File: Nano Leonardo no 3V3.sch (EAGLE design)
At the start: 27 parts, among them U201 5V, U210 3.3V, U401 ATMEGA32U4, X1 USB_MICROB_JSTGCT, Y1 16MHz

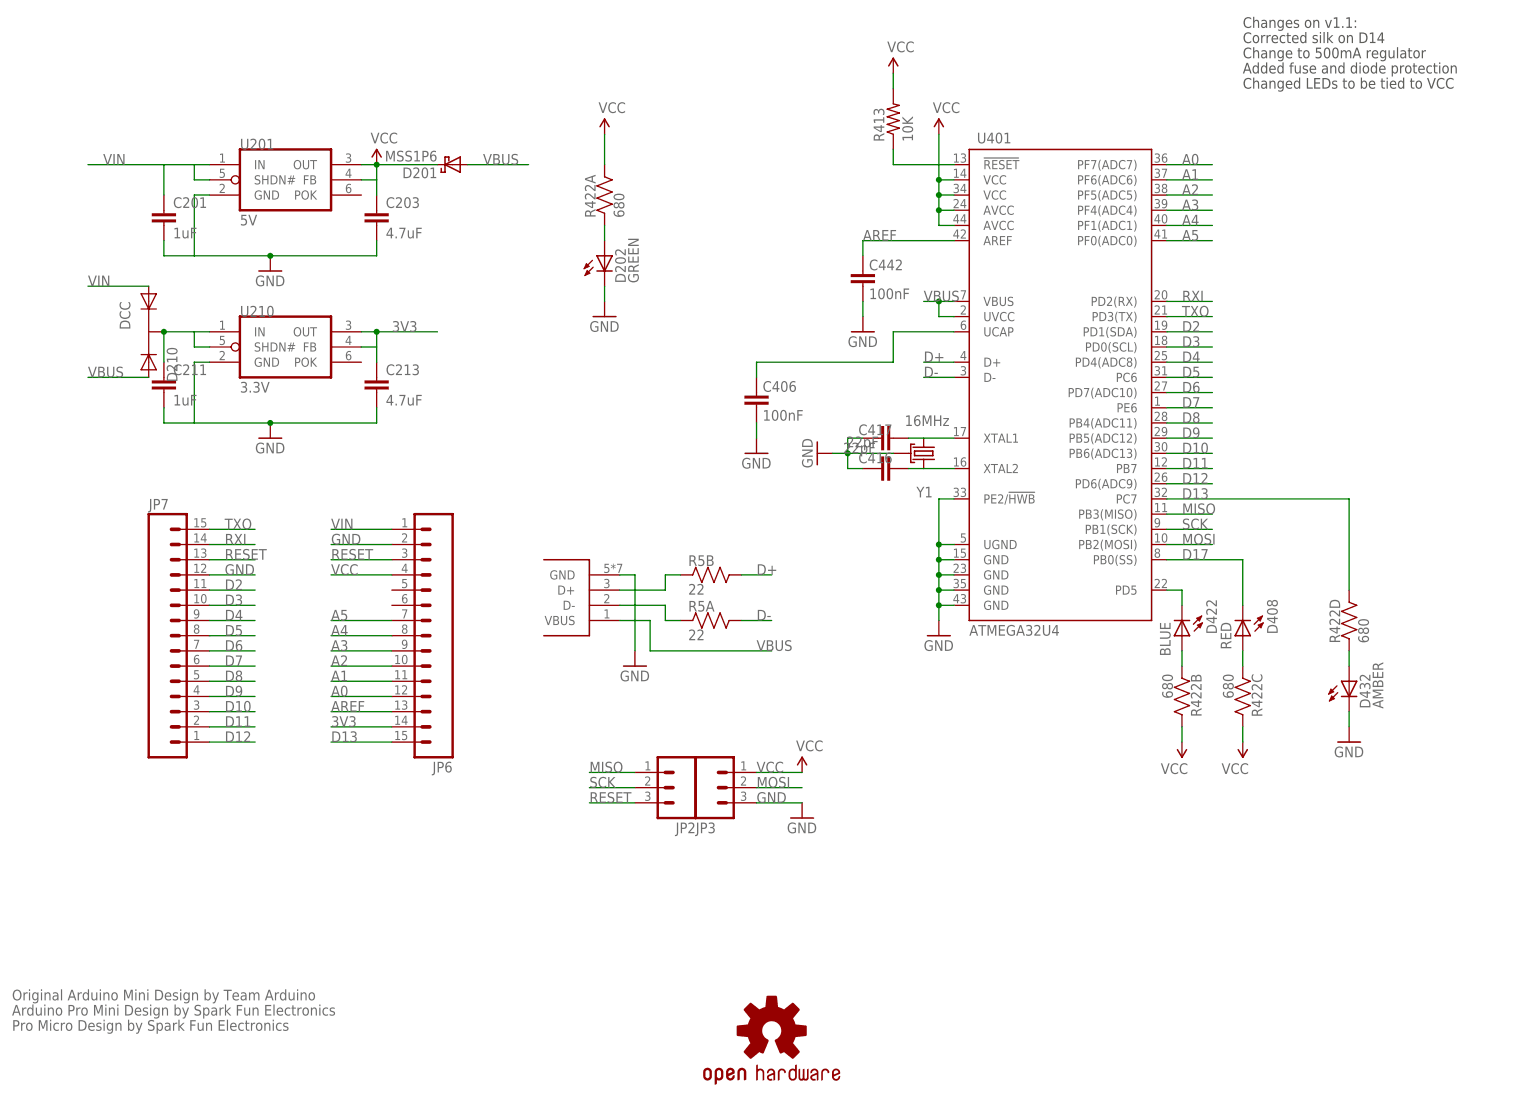
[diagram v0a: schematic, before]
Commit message: Added Nano Leonardo no 3V3
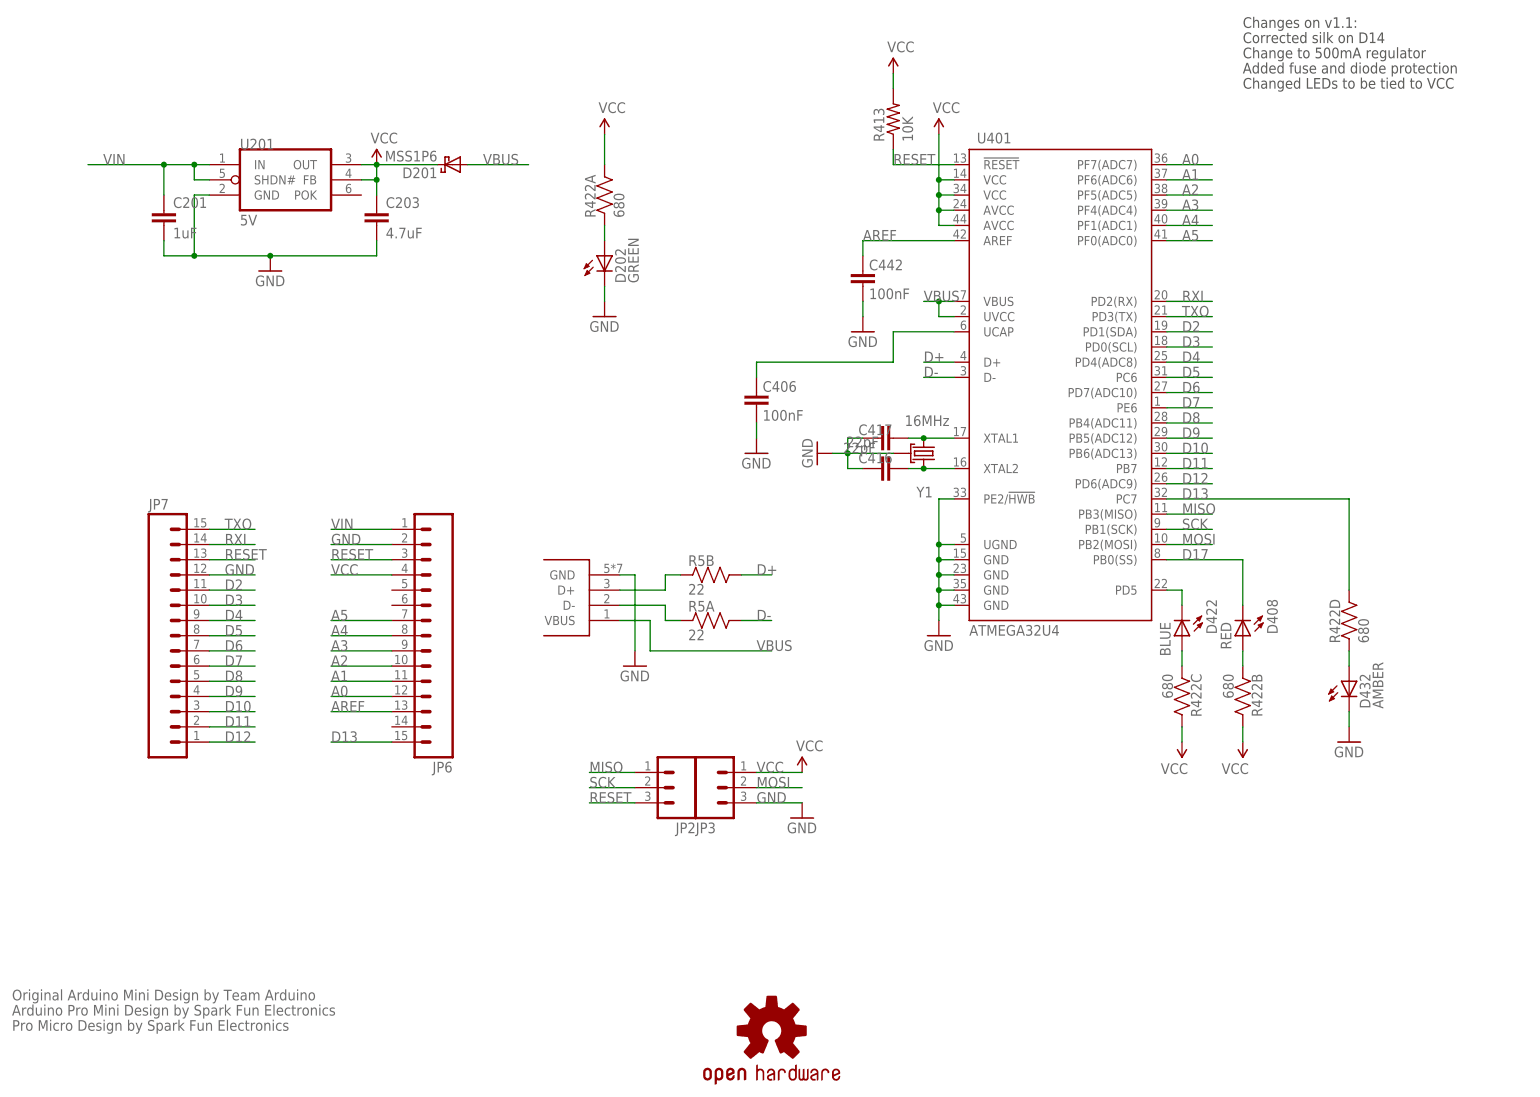
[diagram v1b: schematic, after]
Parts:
- removed C211: 1uF, SparkFun:CAP0402-CAP
- removed C213: 4.7uF, SparkFun:CAP0402-CAP
- removed D210: DCC, KwanSystems:PMEG2005CT
- removed U210: 3.3V, KwanSystems:MAX8881
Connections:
- removed net 3V3: C213.1, JP6.14, U210.FB, U210.OUT
- removed net V3.3SUPPLY: C211.1, D210.K, U210.IN, U210.SHDN#
- net GND: no longer C211.2, C213.2, U210.GND
- net N$1: now also R422C.1; no longer R422B.1
- net N$2: now also R422B.1; no longer R422C.1
- net VBUS: no longer D210.A2
- net VIN: no longer D210.A1
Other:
- moved on the sheet: R422B, R422C
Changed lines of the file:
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@@
 <part name="SUPPLY7" library="SparkFun-Aesthetics" deviceset="VCC" device=""/>
 <part name="SUPPLY8" library="SparkFun-Aesthetics" deviceset="VCC" device=""/>
-<part name="U210" library="KwanSystems" deviceset="MAX8881" device="" value="3.3V">
-<attribute name="DIGIKEY" value="MAX8881EUT50+TCT-ND"/>
-</part>
-<part name="C213" library="SparkFun" deviceset="CAP" device="0402-CAP" value="4.7uF">
-<attribute name="DIGIKEY" value="445-7395-1-ND"/>
-</part>
-<part name="C211" library="SparkFun" deviceset="CAP" device="0402-CAP" value="1uF">
-<attribute name="DIGIKEY" value="445-1415-1-ND"/>
-</part>
-<part name="GND8" library="SparkFun" deviceset="GND" device=""/>
-<part name="D210" library="KwanSystems" deviceset="PMEG2005CT" device="" value="DCC"/>
 <part name="D432" library="SparkFun" deviceset="LED" device="0603" value="AMBER"/>
 <part name="GND9" library="SparkFun" deviceset="GND" device=""/>
@@
 <instance part="R5" gate="A" x="121.92" y="81.28"/>
 <instance part="R422" gate="A" x="104.14" y="152.4" rot="R90"/>
-<instance part="R422" gate="B" x="200.66" y="68.58" rot="R270"/>
-<instance part="R422" gate="C" x="210.82" y="68.58" rot="R270"/>
+<instance part="R422" gate="C" x="200.66" y="68.58" rot="R270"/>
+<instance part="R422" gate="B" x="210.82" y="68.58" rot="R270"/>
 <instance part="GND1" gate="1" x="137.16" y="48.26"/>
 <instance part="SUPPLY1" gate="1" x="152.4" y="172.72"/>
@@
 <instance part="SUPPLY7" gate="1" x="210.82" y="60.96" rot="R180"/>
 <instance part="SUPPLY8" gate="1" x="137.16" y="55.88"/>
-<instance part="U210" gate="G$1" x="50.8" y="127">
-<attribute name="DIGIKEY" x="50.8" y="127" size="1.778" layer="96" display="off"/>
-</instance>
-<instance part="C213" gate="G$1" x="66.04" y="119.38">
-<attribute name="DIGIKEY" x="66.04" y="119.38" size="1.778" layer="96" display="off"/>
-</instance>
-<instance part="C211" gate="G$1" x="30.48" y="119.38">
-<attribute name="DIGIKEY" x="30.48" y="119.38" size="1.778" layer="96" display="off"/>
-</instance>
-<instance part="GND8" gate="1" x="48.26" y="111.76"/>
-<instance part="D210" gate="G$1" x="27.94" y="129.54" rot="R180"/>
 <instance part="D432" gate="G$1" x="228.6" y="71.12"/>
 <instance part="GND9" gate="1" x="228.6" y="60.96"/>
@@
 <wire x1="38.1" y1="152.4" x2="35.56" y2="152.4" width="0.1524" layer="91"/>
 <wire x1="35.56" y1="152.4" x2="35.56" y2="142.24" width="0.1524" layer="91"/>
+<junction x="35.56" y="142.24"/>
 </segment>
 <segment>
@@
 <label x="129.54" y="50.8" size="1.778" layer="95"/>
 <pinref part="JP3" gate="G$1" pin="3"/>
-</segment>
-<segment>
-<pinref part="C211" gate="G$1" pin="2"/>
-<wire x1="30.48" y1="116.84" x2="30.48" y2="114.3" width="0.1524" layer="91"/>
-<wire x1="30.48" y1="114.3" x2="35.56" y2="114.3" width="0.1524" layer="91"/>
-<pinref part="C213" gate="G$1" pin="2"/>
-<wire x1="35.56" y1="114.3" x2="48.26" y2="114.3" width="0.1524" layer="91"/>
-<wire x1="48.26" y1="114.3" x2="66.04" y2="114.3" width="0.1524" layer="91"/>
-<wire x1="66.04" y1="114.3" x2="66.04" y2="116.84" width="0.1524" layer="91"/>
-<pinref part="GND8" gate="1" pin="GND"/>
-<junction x="48.26" y="114.3"/>
-<pinref part="U210" gate="G$1" pin="GND"/>
-<wire x1="38.1" y1="124.46" x2="35.56" y2="124.46" width="0.1524" layer="91"/>
-<wire x1="35.56" y1="124.46" x2="35.56" y2="114.3" width="0.1524" layer="91"/>
 </segment>
 <segment>
@@
 <pinref part="R413" gate="G$1" pin="1"/>
 <pinref part="U401" gate="G$1" pin="!RESET"/>
+<label x="152.4" y="157.48" size="1.778" layer="95"/>
 </segment>
 <segment>
@@
 <pinref part="SUPPLY5" gate="1" pin="VCC"/>
 <junction x="66.04" y="157.48"/>
-</segment>
-<segment>
-<pinref part="R422" gate="B" pin="2"/>
+<junction x="66.04" y="154.94"/>
+</segment>
+<segment>
+<pinref part="R422" gate="C" pin="2"/>
 <pinref part="SUPPLY6" gate="1" pin="VCC"/>
 <wire x1="200.66" y1="63.5" x2="200.66" y2="60.96" width="0.1524" layer="91"/>
 </segment>
 <segment>
-<pinref part="R422" gate="C" pin="2"/>
+<pinref part="R422" gate="B" pin="2"/>
 <pinref part="SUPPLY7" gate="1" pin="VCC"/>
 <wire x1="210.82" y1="63.5" x2="210.82" y2="60.96" width="0.1524" layer="91"/>
@@
 <pinref part="U401" gate="G$1" pin="XTAL1"/>
 <wire x1="157.48" y1="111.76" x2="162.56" y2="111.76" width="0.1524" layer="91"/>
+<junction x="157.48" y="111.76"/>
 </segment>
 </net>
@@
 <wire x1="157.48" y1="106.68" x2="162.56" y2="106.68" width="0.1524" layer="91"/>
 <pinref part="U401" gate="G$1" pin="XTAL2"/>
+<junction x="157.48" y="106.68"/>
 </segment>
 </net>
@@
 <wire x1="35.56" y1="154.94" x2="35.56" y2="157.48" width="0.1524" layer="91"/>
 <label x="20.32" y="157.48" size="1.778" layer="95"/>
+<junction x="30.48" y="157.48"/>
+<junction x="35.56" y="157.48"/>
 </segment>
 <segment>
@@
 <label x="58.42" y="96.52" size="1.778" layer="95"/>
 <pinref part="JP6" gate="G$1" pin="1"/>
-</segment>
-<segment>
-<pinref part="D210" gate="G$1" pin="A1"/>
-<wire x1="27.94" y1="137.16" x2="17.78" y2="137.16" width="0.1524" layer="91"/>
-<label x="17.78" y="137.16" size="1.778" layer="95"/>
 </segment>
 </net>
@@
 <pinref part="X1" gate="G$1" pin="VBUS"/>
 </segment>
-<segment>
-<pinref part="D210" gate="G$1" pin="A2"/>
-<wire x1="27.94" y1="121.92" x2="17.78" y2="121.92" width="0.1524" layer="91"/>
-<label x="17.78" y="121.92" size="1.778" layer="95"/>
-</segment>
-</net>
-<net name="3V3" class="0">
-<segment>
-<pinref part="U210" gate="G$1" pin="FB"/>
-<wire x1="63.5" y1="127" x2="66.04" y2="127" width="0.1524" layer="91"/>
-<wire x1="66.04" y1="127" x2="66.04" y2="129.54" width="0.1524" layer="91"/>
-<pinref part="U210" gate="G$1" pin="OUT"/>
-<wire x1="63.5" y1="129.54" x2="66.04" y2="129.54" width="0.1524" layer="91"/>
-<wire x1="66.04" y1="129.54" x2="76.2" y2="129.54" width="0.1524" layer="91"/>
-<pinref part="C213" gate="G$1" pin="1"/>
-<wire x1="66.04" y1="124.46" x2="66.04" y2="127" width="0.1524" layer="91"/>
-<junction x="66.04" y="129.54"/>
-<label x="68.58" y="129.54" size="1.778" layer="95"/>
-</segment>
-<segment>
-<pinref part="JP6" gate="G$1" pin="14"/>
-<wire x1="68.58" y1="63.5" x2="58.42" y2="63.5" width="0.1524" layer="91"/>
-<label x="58.42" y="63.5" size="1.778" layer="95"/>
-</segment>
-</net>
-<net name="V3.3SUPPLY" class="0">
-<segment>
-<pinref part="U210" gate="G$1" pin="IN"/>
-<wire x1="38.1" y1="129.54" x2="35.56" y2="129.54" width="0.1524" layer="91"/>
-<pinref part="C211" gate="G$1" pin="1"/>
-<wire x1="35.56" y1="129.54" x2="30.48" y2="129.54" width="0.1524" layer="91"/>
-<wire x1="30.48" y1="124.46" x2="30.48" y2="129.54" width="0.1524" layer="91"/>
-<pinref part="U210" gate="G$1" pin="SHDN#"/>
-<wire x1="38.1" y1="127" x2="35.56" y2="127" width="0.1524" layer="91"/>
-<wire x1="35.56" y1="127" x2="35.56" y2="129.54" width="0.1524" layer="91"/>
-<pinref part="D210" gate="G$1" pin="K"/>
-<junction x="30.48" y="129.54"/>
-</segment>
 </net>
 <net name="N$3" class="0">
@@
 <segment>
 <pinref part="D422" gate="G$1" pin="A"/>
+<pinref part="R422" gate="C" pin="1"/>
+<wire x1="200.66" y1="76.2" x2="200.66" y2="73.66" width="0.1524" layer="91"/>
+</segment>
+</net>
+<net name="N$2" class="0">
+<segment>
+<pinref part="D408" gate="G$1" pin="A"/>
 <pinref part="R422" gate="B" pin="1"/>
-<wire x1="200.66" y1="76.2" x2="200.66" y2="73.66" width="0.1524" layer="91"/>
-</segment>
-</net>
-<net name="N$2" class="0">
-<segment>
-<pinref part="D408" gate="G$1" pin="A"/>
-<pinref part="R422" gate="C" pin="1"/>
 <wire x1="210.82" y1="76.2" x2="210.82" y2="73.66" width="0.1524" layer="91"/>
 </segment>

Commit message: Lots of work on Android things
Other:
- moved on the sheet: R5A, R5B
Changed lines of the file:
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@@
 <attribute name="VALUE" x="207.137" y="81.026" size="1.778" layer="96" rot="R270"/>
 </instance>
-<instance part="X1" gate="G$1" x="101.6" y="86.36" rot="MR0"/>
+<instance part="X1" gate="G$1" x="101.6" y="83.82" rot="R180"/>
 <instance part="GND3" gate="1" x="109.22" y="73.66"/>
 <instance part="U201" gate="G$1" x="50.8" y="154.94">
@@
 </instance>
 <instance part="GND5" gate="1" x="48.26" y="139.7"/>
-<instance part="R5" gate="B" x="121.92" y="88.9"/>
-<instance part="R5" gate="A" x="121.92" y="81.28"/>
+<instance part="R5" gate="B" x="119.38" y="83.82"/>
+<instance part="R5" gate="A" x="119.38" y="86.36"/>
 <instance part="R422" gate="A" x="104.14" y="152.4" rot="R90"/>
 <instance part="R422" gate="C" x="200.66" y="68.58" rot="R270"/>
@@
 </segment>
 <segment>
-<wire x1="106.68" y1="88.9" x2="109.22" y2="88.9" width="0.1524" layer="91"/>
-<wire x1="109.22" y1="88.9" x2="109.22" y2="76.2" width="0.1524" layer="91"/>
+<wire x1="106.68" y1="81.28" x2="109.22" y2="81.28" width="0.1524" layer="91"/>
+<wire x1="109.22" y1="81.28" x2="109.22" y2="76.2" width="0.1524" layer="91"/>
 <pinref part="X1" gate="G$1" pin="GND"/>
 <pinref part="GND3" gate="1" pin="GND"/>
@@
 </segment>
 <segment>
-<wire x1="127" y1="81.28" x2="132.08" y2="81.28" width="0.1524" layer="91"/>
-<label x="129.54" y="81.28" size="1.778" layer="95"/>
+<wire x1="124.46" y1="86.36" x2="129.54" y2="86.36" width="0.1524" layer="91"/>
+<label x="127" y="86.36" size="1.778" layer="95"/>
 <pinref part="R5" gate="A" pin="2"/>
 </segment>
@@
 </segment>
 <segment>
-<wire x1="127" y1="88.9" x2="132.08" y2="88.9" width="0.1524" layer="91"/>
-<label x="129.54" y="88.9" size="1.778" layer="95"/>
+<wire x1="124.46" y1="83.82" x2="129.54" y2="83.82" width="0.1524" layer="91"/>
+<label x="127" y="83.82" size="1.778" layer="95"/>
 <pinref part="R5" gate="B" pin="2"/>
 </segment>
@@
 <net name="N$6" class="0">
 <segment>
-<wire x1="106.68" y1="83.82" x2="114.3" y2="83.82" width="0.1524" layer="91"/>
-<wire x1="114.3" y1="83.82" x2="114.3" y2="81.28" width="0.1524" layer="91"/>
-<wire x1="114.3" y1="81.28" x2="116.84" y2="81.28" width="0.1524" layer="91"/>
+<wire x1="106.68" y1="86.36" x2="114.3" y2="86.36" width="0.1524" layer="91"/>
 <pinref part="X1" gate="G$1" pin="D-"/>
 <pinref part="R5" gate="A" pin="1"/>
@@
 <net name="N$8" class="0">
 <segment>
-<wire x1="106.68" y1="86.36" x2="114.3" y2="86.36" width="0.1524" layer="91"/>
-<wire x1="114.3" y1="86.36" x2="114.3" y2="88.9" width="0.1524" layer="91"/>
-<wire x1="114.3" y1="88.9" x2="116.84" y2="88.9" width="0.1524" layer="91"/>
+<wire x1="106.68" y1="83.82" x2="114.3" y2="83.82" width="0.1524" layer="91"/>
 <pinref part="X1" gate="G$1" pin="D+"/>
 <pinref part="R5" gate="B" pin="1"/>
@@
 </segment>
 <segment>
-<wire x1="106.68" y1="81.28" x2="111.76" y2="81.28" width="0.1524" layer="91"/>
-<wire x1="111.76" y1="81.28" x2="111.76" y2="76.2" width="0.1524" layer="91"/>
-<wire x1="111.76" y1="76.2" x2="132.08" y2="76.2" width="0.1524" layer="91"/>
-<label x="129.54" y="76.2" size="1.778" layer="95"/>
+<wire x1="106.68" y1="88.9" x2="129.54" y2="88.9" width="0.1524" layer="91"/>
+<label x="124.46" y="88.9" size="1.778" layer="95"/>
 <pinref part="X1" gate="G$1" pin="VBUS"/>
 </segment>
